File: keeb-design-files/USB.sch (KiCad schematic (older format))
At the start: 25 parts, among them J3 USB_B, J4 S2B-PH-K-S, J5 Conn_01x02, SW71 SW_SPDT, U3 USBLC6-2SC6, U4 BQ24075, U5 NXE2S0505MC

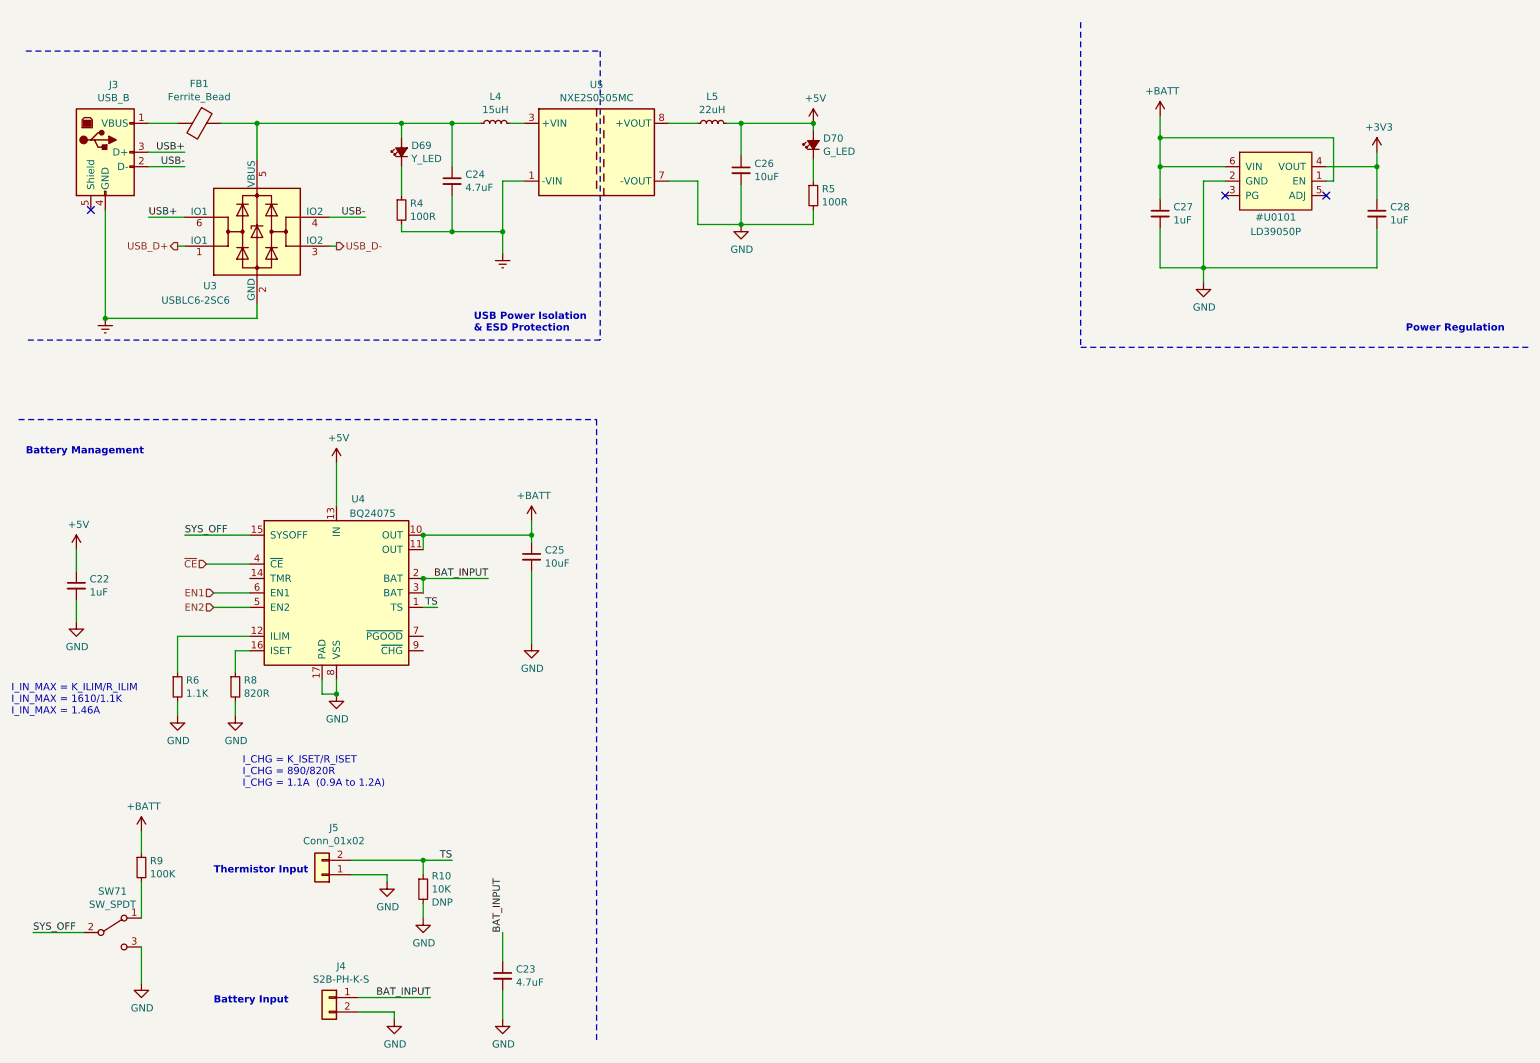
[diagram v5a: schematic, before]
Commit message: Add I2C Pull-ups, Add STC3100 Fuel Guage
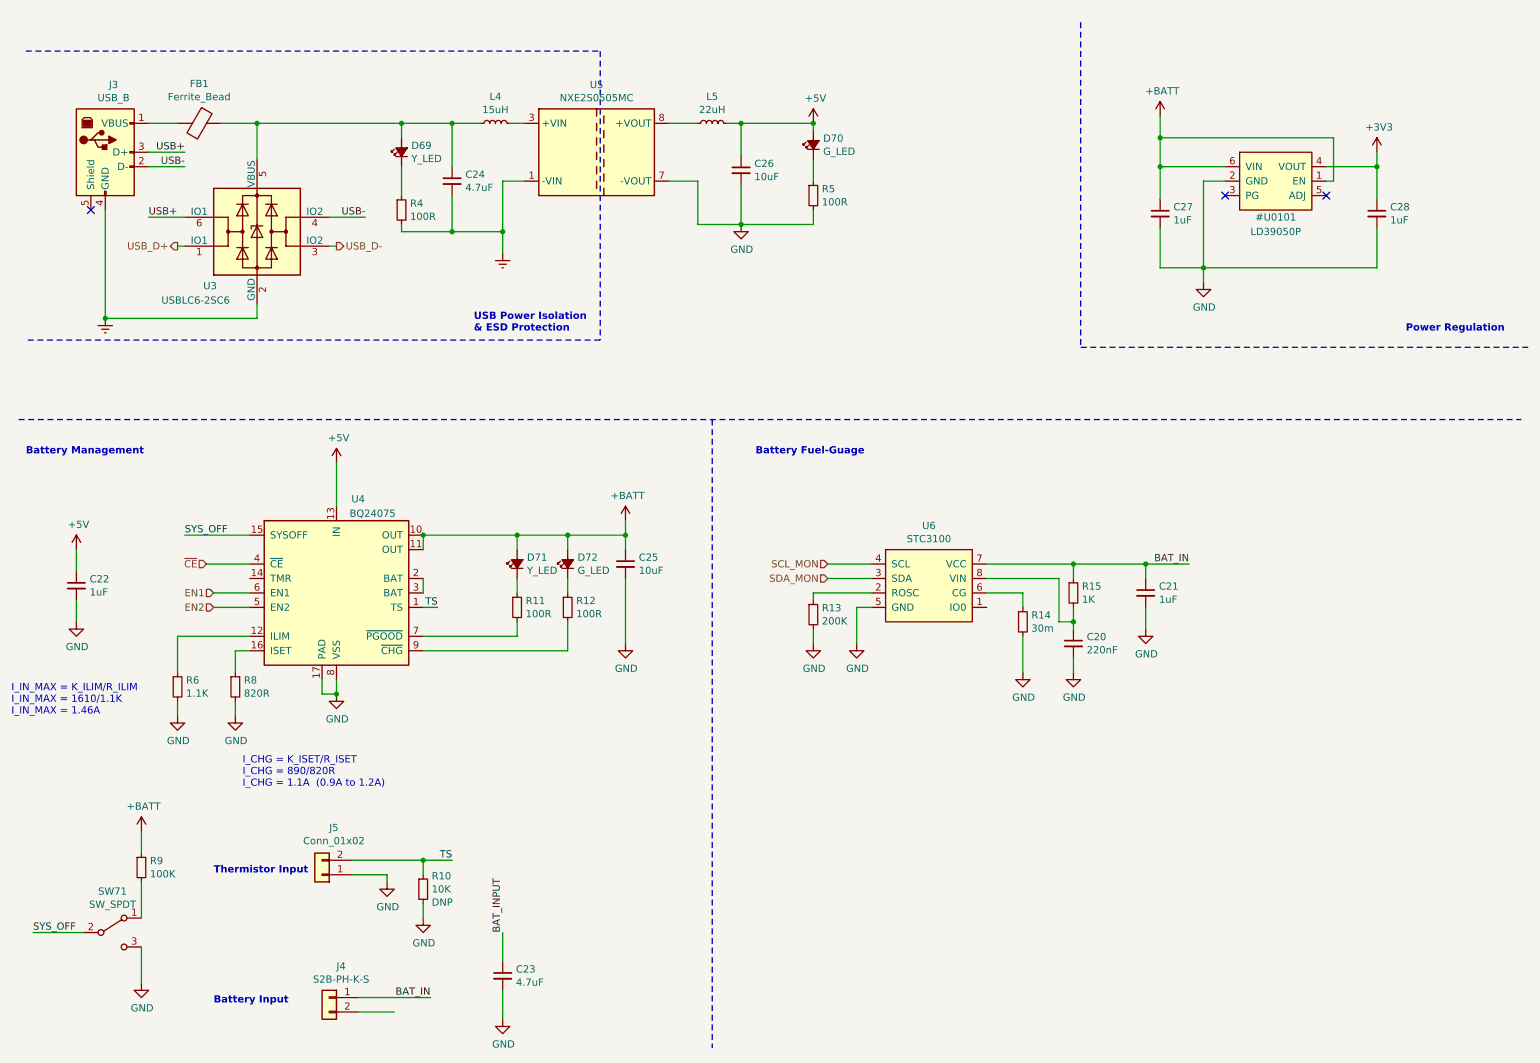
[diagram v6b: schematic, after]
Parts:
- added C20: 220nF, symbol Device:C_Small
- added C21: 1uF, symbol Device:C_Small
- added D71: Y_LED, LED_SMD:LED_0603_1608Metric, symbol Device:LED_Small_ALT
- added D72: G_LED, LED_SMD:LED_0603_1608Metric, symbol Device:LED_Small_ALT
- added R11, R12: 100R, Resistor_SMD:R_0402_1005Metric, symbol Device:R_Small
- added R13: 200K, symbol Device:R_Small
- added R14: 30m, Resistor_SMD:R_0805_2012Metric, symbol Device:R_Small
- added R15: 1K, symbol Device:R_Small
- added U6: STC3100, symbol PMIC:STC3100
- U4: footprint Package_DFN_QFN:QFN-16-1EP_3x3mm_P0.5mm_EP1.7x1.7mm -> lib_fp:QFN-16-1EP_3x3mm_P0.5mm_EP1.7x1.7mm
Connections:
- net +BATT: now also D71.2 (A), D72.2 (A)
- net BAT_INPUT: no longer J4.1 (Pin_1), U4.2 (BAT), U4.3 (BAT)
- net GND: now also C20.2, C21.2, R13.2, R14.2, U6.5 (GND); no longer J4.2 (Pin_2)
- net at U4.7 (~PGOOD): now also R11.2
- net at U4.9 (~CHG): now also R12.2
- new net: D71.1 (K), R11.1
- new net: D72.1 (K), R12.1
- new net: R13.1, U6.2 (ROSC)
- new net: R14.1, U6.6 (CG)
- new net: C20.1, R15.2, U6.8 (VIN)
- new net: U4.2 (BAT), U4.3 (BAT)
- new net BAT_IN: C21.1, J4.1 (Pin_1), R15.1, U6.7 (VCC)
- new net SCL_MON: U6.4 (SCL)
- new net SDA_MON: U6.3 (SDA)
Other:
- note added: "Battery Fuel-Guage"
- moved on the sheet: C25

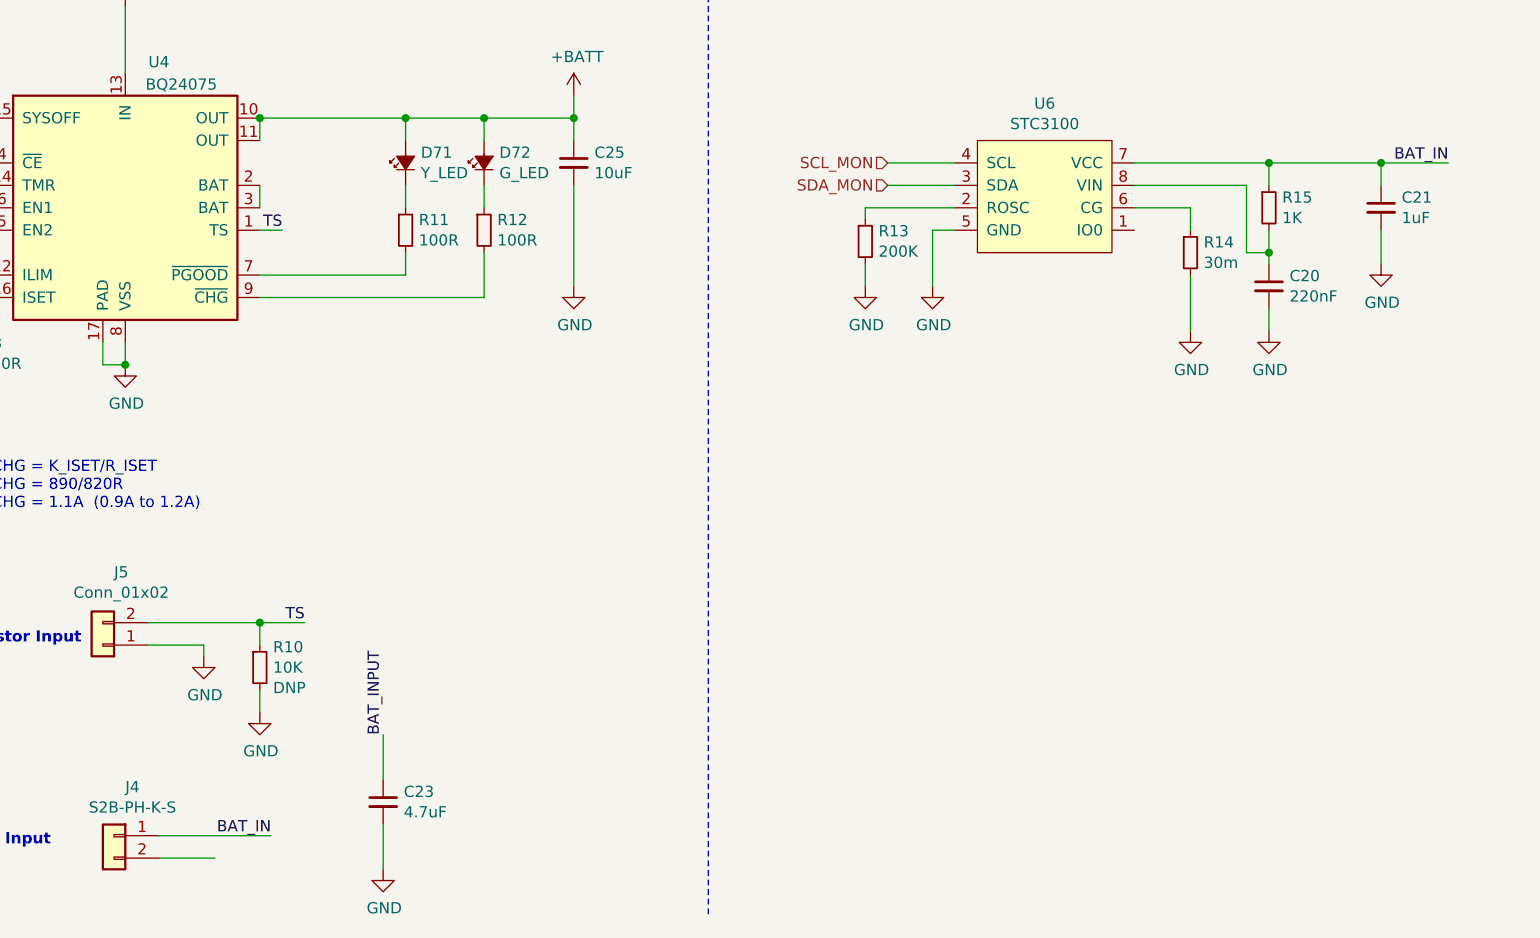
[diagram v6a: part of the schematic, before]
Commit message: Fix minor Batter Management issue
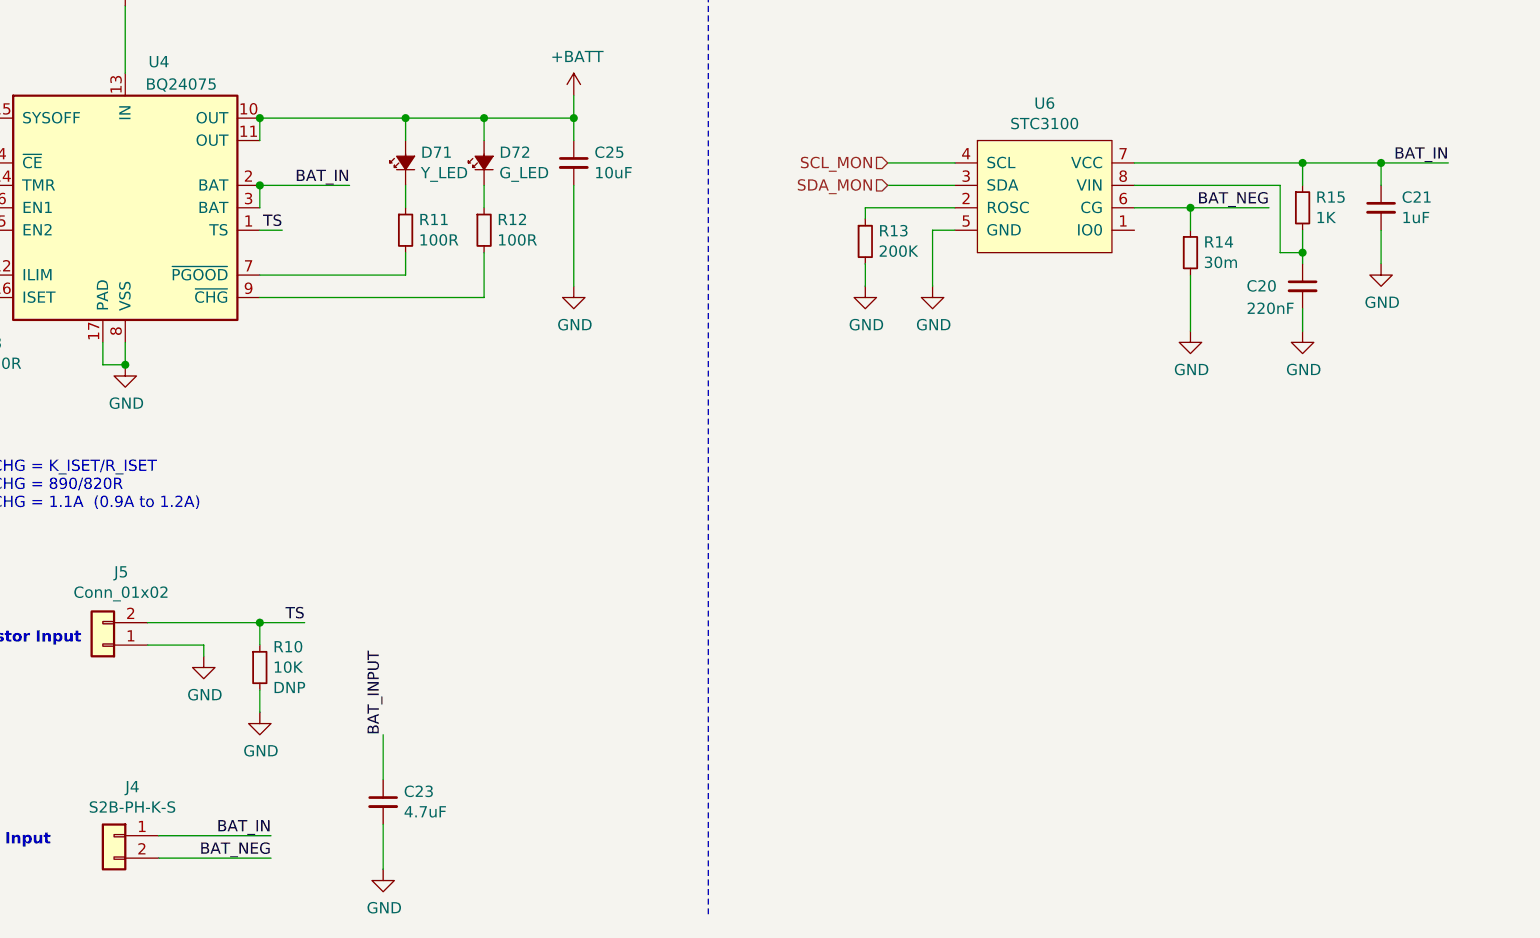
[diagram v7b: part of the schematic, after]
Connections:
- net BAT_IN: now also U4.2 (BAT), U4.3 (BAT)
- net BAT_NEG: now reaches J4.2 (Pin_2)
- net BAT_NEG: now also R14.1, U6.6 (CG)
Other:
- moved on the sheet: C20, R15
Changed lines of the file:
@@
 	-1   0    0    -1
 $EndComp
-Wire Wire Line
-	3250 7450 3000 7450
 Text HLabel 2000 4550 0    50   Input ~ 0
 EN1
@@
 L Device:R_Small R15
 U 1 1 5ECB3C4C
-P 7950 4550
-F 0 "R15" H 8009 4596 50  0000 L CNN
-F 1 "1K" H 8009 4505 50  0000 L CNN
-F 2 "" H 7950 4550 50  0001 C CNN
-F 3 "~" H 7950 4550 50  0001 C CNN
-	1    7950 4550
+P 8100 4550
+F 0 "R15" H 8159 4596 50  0000 L CNN
+F 1 "1K" H 8159 4505 50  0000 L CNN
+F 2 "" H 8100 4550 50  0001 C CNN
+F 3 "~" H 8100 4550 50  0001 C CNN
+	1    8100 4550
 	1    0    0    -1
 $EndComp
@@
 L Device:C_Small C20
 U 1 1 5ECB4C56
-P 7950 4900
-F 0 "C20" H 8042 4946 50  0000 L CNN
-F 1 "220nF" H 8042 4855 50  0000 L CNN
-F 2 "" H 7950 4900 50  0001 C CNN
-F 3 "~" H 7950 4900 50  0001 C CNN
-	1    7950 4900
+P 8100 4900
+F 0 "C20" H 7850 4900 50  0000 L CNN
+F 1 "220nF" H 7850 4800 50  0000 L CNN
+F 2 "" H 8100 4900 50  0001 C CNN
+F 3 "~" H 8100 4900 50  0001 C CNN
+	1    8100 4900
 	1    0    0    -1
 $EndComp
@@
 L power:GND #PWR0149
 U 1 1 5ECB563A
-P 7950 5100
-F 0 "#PWR0149" H 7950 4850 50  0001 C CNN
-F 1 "GND" H 7955 4927 50  0000 C CNN
-F 2 "" H 7950 5100 50  0001 C CNN
-F 3 "" H 7950 5100 50  0001 C CNN
-	1    7950 5100
-	1    0    0    -1
-$EndComp
-Wire Wire Line
-	7950 4450 7950 4350
-Connection ~ 7950 4350
-Wire Wire Line
-	7950 4350 7350 4350
+P 8100 5100
+F 0 "#PWR0149" H 8100 4850 50  0001 C CNN
+F 1 "GND" H 8105 4927 50  0000 C CNN
+F 2 "" H 8100 5100 50  0001 C CNN
+F 3 "" H 8100 5100 50  0001 C CNN
+	1    8100 5100
+	1    0    0    -1
+$EndComp
+Wire Wire Line
+	8100 4450 8100 4350
+Connection ~ 8100 4350
+Wire Wire Line
+	8100 4350 7350 4350
 Wire Wire Line
 	8450 4350 8450 4450
 Connection ~ 8450 4350
 Wire Wire Line
-	8450 4350 7950 4350
-Wire Wire Line
-	7950 4650 7950 4750
-Wire Wire Line
-	7950 5000 7950 5100
+	8450 4350 8100 4350
+Wire Wire Line
+	8100 4650 8100 4750
+Wire Wire Line
+	8100 5000 8100 5100
 $Comp
 L power:GND #PWR0150
@@
 	8450 4800 8450 4650
 Wire Wire Line
-	7350 4450 7850 4450
-Wire Wire Line
-	7850 4450 7850 4750
-Wire Wire Line
-	7850 4750 7950 4750
-Connection ~ 7950 4750
-Wire Wire Line
-	7950 4750 7950 4800
+	7350 4450 8000 4450
+Wire Wire Line
+	8000 4450 8000 4750
+Wire Wire Line
+	8000 4750 8100 4750
+Connection ~ 8100 4750
+Wire Wire Line
+	8100 4750 8100 4800
 Text HLabel 6250 4350 0    50   Input ~ 0
 SCL_MON
@@
 Text Notes 5750 3600 0    50   ~ 10
 Battery Fuel-Guage
+Text Label 7950 4550 2    50   ~ 0
+BAT_NEG
+Wire Wire Line
+	7950 4550 7600 4550
+Connection ~ 7600 4550
+Text Label 3500 7450 2    50   ~ 0
+BAT_NEG
+Wire Wire Line
+	3000 7450 3500 7450
+Text Label 3850 4450 2    50   ~ 0
+BAT_IN
+Wire Wire Line
+	3450 4450 3850 4450
+Connection ~ 3450 4450
 $EndSCHEMATC
